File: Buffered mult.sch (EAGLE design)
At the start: 29 parts, among them IC1 OPA4171, IC3 OPA4171, J1 EURO_POWER_HEADERFAT_PADS

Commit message: fixed error in schematic
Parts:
- R1, R2, R3, R4, R5, R6, R9: value 1k -> 51
- R7, R8: value 4.7m -> 10m
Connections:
- net N$2: now also IC1A.-IN; no longer IC1A.+IN
- net N$5: now also IC1A.+IN; no longer IC1A.-IN
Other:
- note added: "Inspired by Mutable Instruments LINKS"
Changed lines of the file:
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@@
 </classes>
 <parts>
-<part name="R1" library="SparkFun-Passives" deviceset="RESISTOR" device="1206" value="1k"/>
-<part name="R2" library="SparkFun-Passives" deviceset="RESISTOR" device="1206" value="1k"/>
-<part name="R3" library="SparkFun-Passives" deviceset="RESISTOR" device="1206" value="1k"/>
-<part name="R4" library="SparkFun-Passives" deviceset="RESISTOR" device="1206" value="1k"/>
-<part name="R5" library="SparkFun-Passives" deviceset="RESISTOR" device="1206" value="1k"/>
-<part name="R6" library="SparkFun-Passives" deviceset="RESISTOR" device="1206" value="1k"/>
+<part name="R1" library="SparkFun-Passives" deviceset="RESISTOR" device="1206" value="51"/>
+<part name="R2" library="SparkFun-Passives" deviceset="RESISTOR" device="1206" value="51"/>
+<part name="R3" library="SparkFun-Passives" deviceset="RESISTOR" device="1206" value="51"/>
+<part name="R4" library="SparkFun-Passives" deviceset="RESISTOR" device="1206" value="51"/>
+<part name="R5" library="SparkFun-Passives" deviceset="RESISTOR" device="1206" value="51"/>
+<part name="R6" library="SparkFun-Passives" deviceset="RESISTOR" device="1206" value="51"/>
 <part name="C1" library="rcl" deviceset="CPOL-US" device="D" value="47u"/>
 <part name="C13" library="rcl" deviceset="CPOL-US" device="D" value="47u"/>
@@
 <part name="GND8" library="SparkFun" deviceset="GND" device=""/>
 <part name="GND9" library="SparkFun" deviceset="GND" device=""/>
-<part name="R7" library="SparkFun-Passives" deviceset="RESISTOR" device="1206" value="4.7m"/>
-<part name="R8" library="SparkFun-Passives" deviceset="RESISTOR" device="1206" value="4.7m"/>
+<part name="R7" library="SparkFun-Passives" deviceset="RESISTOR" device="1206" value="10m"/>
+<part name="R8" library="SparkFun-Passives" deviceset="RESISTOR" device="1206" value="10m"/>
 <part name="GND10" library="SparkFun" deviceset="GND" device=""/>
 <part name="GND11" library="SparkFun" deviceset="GND" device=""/>
@@
 <part name="GND15" library="SparkFun" deviceset="GND" device=""/>
 <part name="IC3" library="linear" deviceset="TL074" device="PW" value="OPA4171"/>
-<part name="R9" library="SparkFun-Passives" deviceset="RESISTOR" device="1206" value="1k"/>
+<part name="R9" library="SparkFun-Passives" deviceset="RESISTOR" device="1206" value="51"/>
 <part name="GND16" library="SparkFun" deviceset="GND" device=""/>
 </parts>
@@
 are 4 outputs part of the
 total 1:7 mult</text>
+<text x="167.64" y="7.62" size="1.778" layer="91">Inspired by Mutable Instruments LINKS</text>
 </plain>
 <instances>
@@
 <wire x1="40.64" y1="144.78" x2="40.64" y2="127" width="0.1524" layer="91"/>
 <wire x1="40.64" y1="127" x2="55.88" y2="127" width="0.1524" layer="91"/>
-<wire x1="40.64" y1="127" x2="40.64" y2="170.18" width="0.1524" layer="91"/>
 <junction x="40.64" y="127"/>
-<wire x1="55.88" y1="170.18" x2="40.64" y2="170.18" width="0.1524" layer="91"/>
 <wire x1="40.64" y1="127" x2="40.64" y2="99.06" width="0.1524" layer="91"/>
 <pinref part="R7" gate="G$1" pin="2"/>
 <wire x1="27.94" y1="137.16" x2="27.94" y2="144.78" width="0.1524" layer="91"/>
 <junction x="27.94" y="144.78"/>
-<pinref part="IC1" gate="A" pin="-IN"/>
 <pinref part="IN1" gate="G$1" pin="TIP"/>
 <pinref part="IC1" gate="B" pin="+IN"/>
@@
 <wire x1="40.64" y1="99.06" x2="55.88" y2="99.06" width="0.1524" layer="91"/>
 <wire x1="55.88" y1="99.06" x2="55.88" y2="96.52" width="0.1524" layer="91"/>
+<wire x1="40.64" y1="144.78" x2="40.64" y2="165.1" width="0.1524" layer="91"/>
+<pinref part="IC1" gate="A" pin="+IN"/>
+<wire x1="40.64" y1="165.1" x2="55.88" y2="165.1" width="0.1524" layer="91"/>
 </segment>
 </net>
@@
 <segment>
 <pinref part="R3" gate="G$1" pin="1"/>
-<wire x1="96.52" y1="167.64" x2="81.28" y2="167.64" width="0.1524" layer="91"/>
-<wire x1="81.28" y1="167.64" x2="71.12" y2="167.64" width="0.1524" layer="91"/>
-<wire x1="55.88" y1="165.1" x2="55.88" y2="154.94" width="0.1524" layer="91"/>
-<wire x1="55.88" y1="154.94" x2="81.28" y2="154.94" width="0.1524" layer="91"/>
-<wire x1="81.28" y1="154.94" x2="81.28" y2="167.64" width="0.1524" layer="91"/>
-<junction x="81.28" y="167.64"/>
-<pinref part="IC1" gate="A" pin="+IN"/>
+<wire x1="96.52" y1="167.64" x2="76.2" y2="167.64" width="0.1524" layer="91"/>
 <pinref part="IC1" gate="A" pin="OUT"/>
-</segment>
-</net>
+<wire x1="76.2" y1="167.64" x2="71.12" y2="167.64" width="0.1524" layer="91"/>
+<wire x1="76.2" y1="167.64" x2="76.2" y2="180.34" width="0.1524" layer="91"/>
+<junction x="76.2" y="167.64"/>
+<wire x1="76.2" y1="180.34" x2="53.34" y2="180.34" width="0.1524" layer="91"/>
+<wire x1="53.34" y1="180.34" x2="53.34" y2="170.18" width="0.1524" layer="91"/>
+<pinref part="IC1" gate="A" pin="-IN"/>
+<wire x1="53.34" y1="170.18" x2="55.88" y2="170.18" width="0.1524" layer="91"/>
+</segment>
+</net>

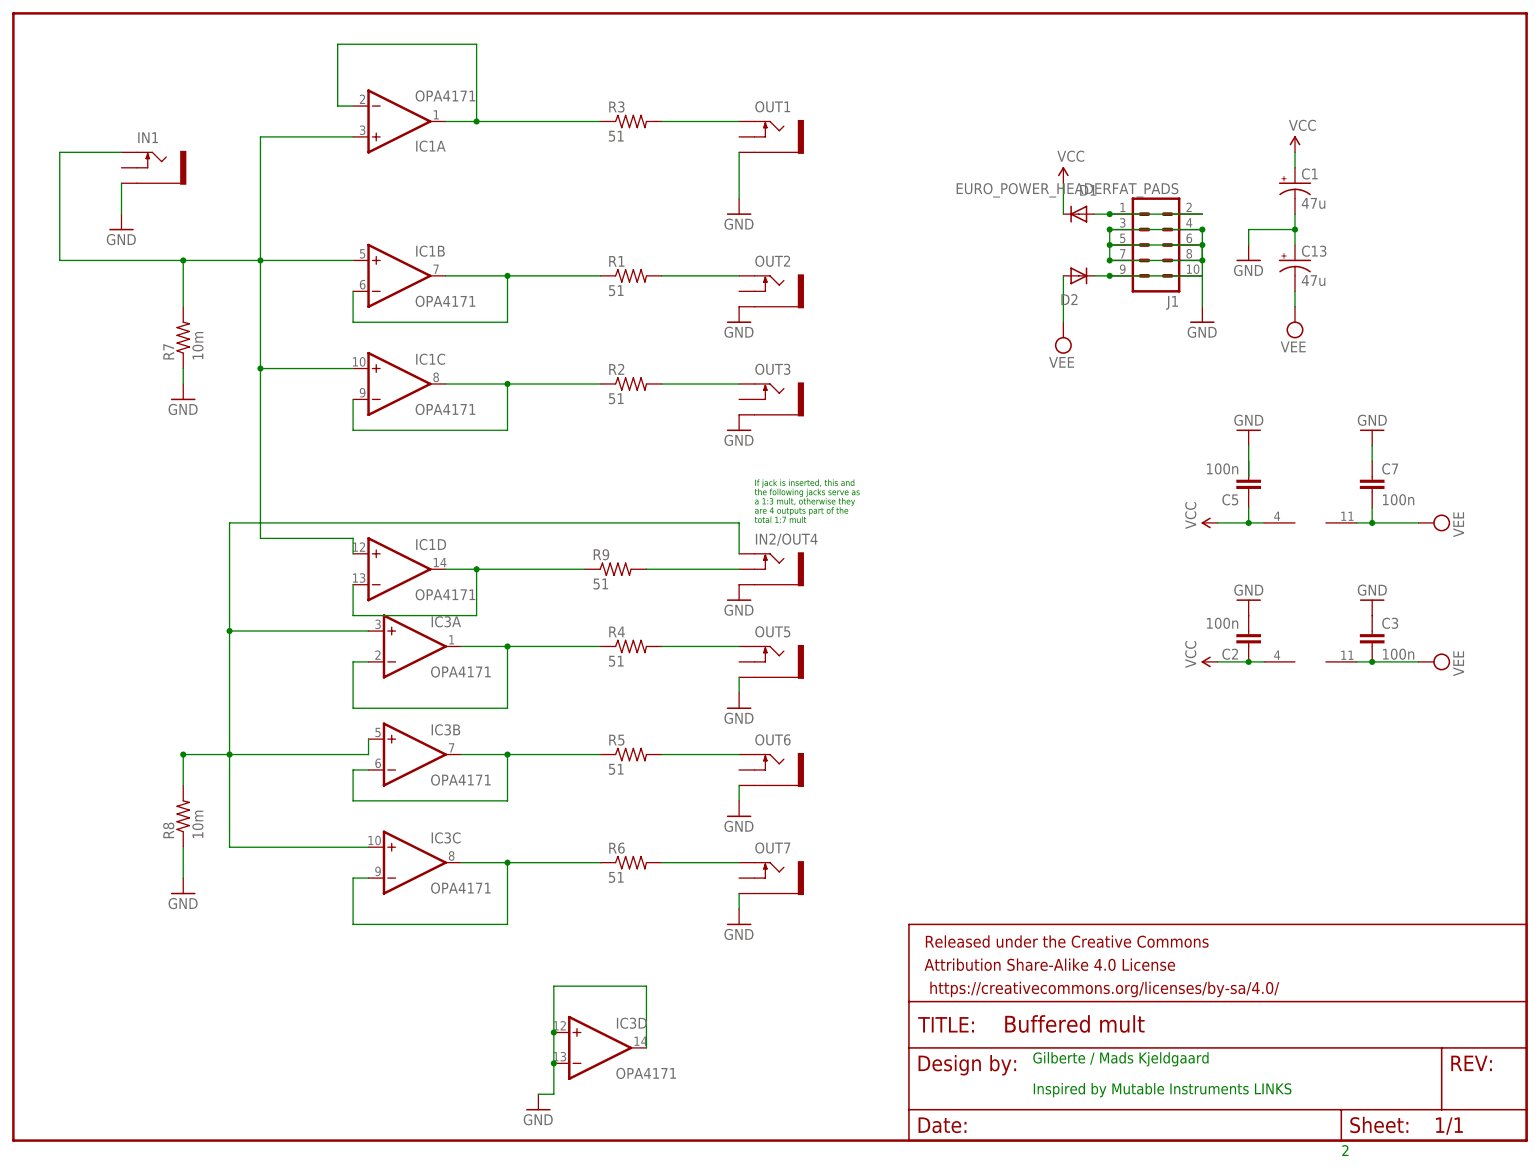
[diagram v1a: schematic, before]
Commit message: new revision: Changed IC2 to opa2171, fixed switch jack
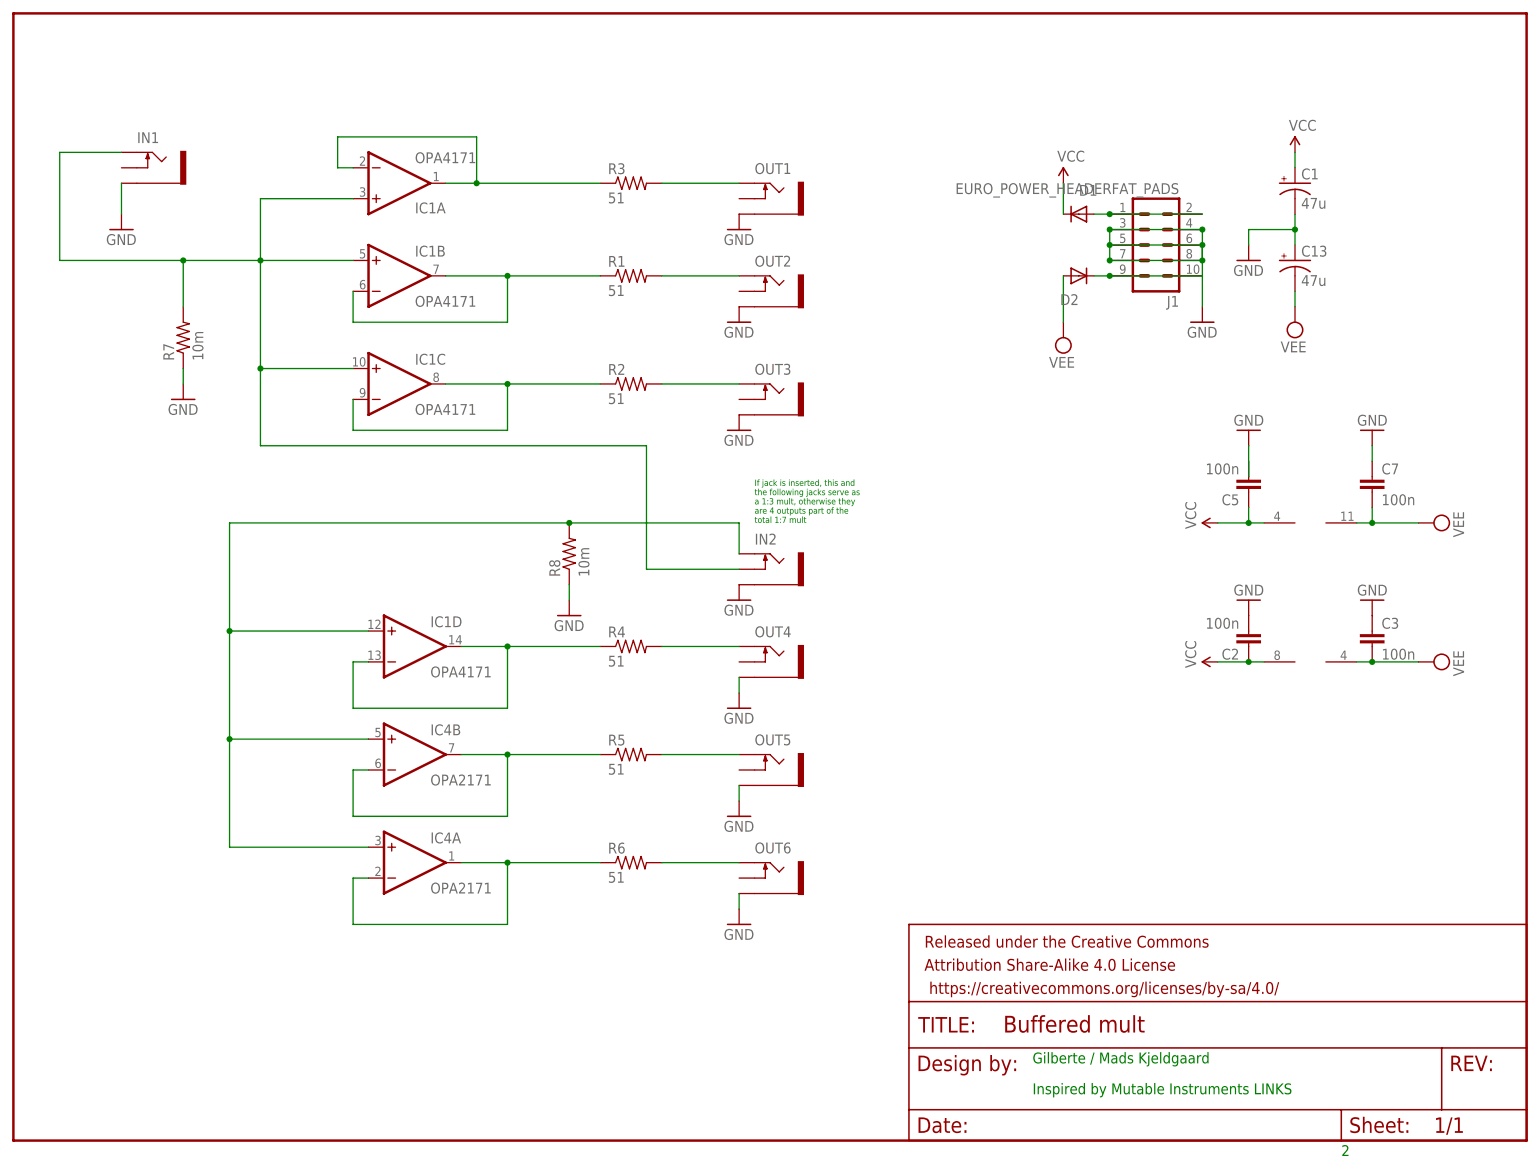
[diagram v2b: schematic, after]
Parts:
- removed IC3: OPA4171, linear:TL074PW
- removed OUT7: PJ302M, pj302m:PJ302M
- removed R9: 51, SparkFun-Passives:RESISTOR1206
- added IC4: OPA2171, linear:TL072D
- added OUT4: PJ302M, pj302m:PJ302M
- renumbered IN2/OUT4 to IN2
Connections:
- removed net N$16: IC1D.-IN, IC1D.OUT, R9.1
- removed net N$18: IN2.SWITCH, R9.2
- net GND: now also OUT4.SLEEVE; no longer IC3D.+IN, IC3D.-IN, IC3D.OUT, OUT7.SLEEVE
- net N$1: now also OUT6.TIP; no longer OUT7.TIP
- net N$12: now also IC4A.-IN, IC4A.OUT; no longer IC3C.-IN, IC3C.OUT
- net N$13: now also IC4B.-IN, IC4B.OUT; no longer IC3B.-IN, IC3B.OUT
- net N$17: now also IC1D.-IN, IC1D.OUT; no longer IC3A.-IN, IC3A.OUT
- net N$19: now also IC1D.+IN, IC4A.+IN, IC4B.+IN; no longer IC3A.+IN, IC3B.+IN, IC3C.+IN
- net N$3: now also OUT5.TIP; no longer OUT6.TIP
- net N$4: now also OUT4.TIP; no longer OUT5.TIP
- net N$5: now also IN2.SWITCH; no longer IC1D.+IN
- net VCC: now also IC4P.V+; no longer IC3P.V+
- net VEE: now also IC4P.V-; no longer IC3P.V-
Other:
- moved on the sheet: IC1A, IC1D, OUT1, OUT5, OUT6, R3, R8

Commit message: small touchups
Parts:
- removed FRAME1: FRAME-LETTER, SparkFun-Aesthetics:FRAME-LETTER
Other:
- note removed: "Gilberte / Mads Kjeldgaard"
- note removed: "Inspired by Mutable Instruments LINKS"
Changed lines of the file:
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@@
 <part name="P+1" library="SparkFun" deviceset="VCC" device=""/>
 <part name="J1" library="MusicThingModular" deviceset="EURO_POWER_HEADER" device="FAT_PADS"/>
-<part name="FRAME1" library="SparkFun-Aesthetics" deviceset="FRAME-LETTER" device=""/>
 <part name="C5" library="SparkFun-Capacitors" deviceset="CAP" device="1206" value="100n"/>
 <part name="C7" library="SparkFun-Capacitors" deviceset="CAP" device="1206" value="100n"/>
@@
 <part name="GND15" library="SparkFun" deviceset="GND" device=""/>
 <part name="IC4" library="linear" deviceset="TL072" device="D" value="OPA2171"/>
+<part name="U$1" library="GeekAmmo" deviceset="FRAME2-A4" device=""/>
 </parts>
 <sheets>
@@
 <description>yo</description>
 <plain>
-<text x="167.64" y="12.7" size="1.778" layer="91">Gilberte / Mads Kjeldgaard</text>
 <text x="218.44" y="-2.54" size="1.778" layer="91">2</text>
 <text x="121.92" y="101.6" size="1.016" layer="91">If jack is inserted, this and
@@
 are 4 outputs part of the
 total 1:7 mult</text>
-<text x="167.64" y="7.62" size="1.778" layer="91">Inspired by Mutable Instruments LINKS</text>
 </plain>
 <instances>
@@
 <instance part="P+1" gate="1" x="198.12" y="78.74" rot="R90"/>
 <instance part="J1" gate="G$1" x="187.96" y="147.32" rot="R180"/>
-<instance part="FRAME1" gate="G$1" x="0" y="0"/>
-<instance part="FRAME1" gate="V" x="147.32" y="0"/>
 <instance part="C5" gate="G$1" x="203.2" y="109.22" rot="R180"/>
 <instance part="C7" gate="G$1" x="223.52" y="106.68"/>
@@
 <instance part="IC4" gate="A" x="66.04" y="45.72"/>
 <instance part="IC4" gate="P" x="213.36" y="78.74" rot="R90"/>
+<instance part="U$1" gate="G$1" x="-2.54" y="15.24"/>
 </instances>
 <busses>
